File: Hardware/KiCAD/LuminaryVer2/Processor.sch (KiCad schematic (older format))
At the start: 18 parts, among them SW1 SW_Push, U2 STM32L432KBUx, U6 AT25SF081-SSHD-X

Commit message: Updated version 2 hardware schematics.
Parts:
- removed R_PWR_3: 0, Resistor_SMD:R_0402_1005Metric, symbol Device:R_US
- added C12, C14: 1uF, Capacitor_SMD:C_0805_2012Metric, symbol Device:C_Small
- added D3, D4: BLED, Diode_SMD:D_0603_1608Metric, symbol Device:LED
- added R16, R17, R18: 1k, Resistor_SMD:R_0402_1005Metric, symbol Device:R_US
- added U10: CP2104, Package_DFN_QFN:QFN-24-1EP_4x4mm_P0.5mm_EP2.6x2.6mm, symbol Interface_USB:CP2104
- D10: LCSC C205443 -> C72043; PartNumber ORH-G36G -> 19-217/GHC-YR1S2/3T
- R11, R3, R32: LCSC C102759 -> C25744
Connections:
- net GND: now also C12.1, C14.2, U10.2 (GND), U10.25 (PAD)
- net RS232_1_RX: now also U10.21 (TXD)
- net RS232_1_TX: now also U10.20 (RXD)
- net VCC: now also C2.2, U6.3 (~WP~/IO2), U6.7 (~HOLD~/IO3), U6.8 (VCC)
- new net: C14.1, R18.2, U10.10 (VIO/NC), U10.5 (VIO), U10.6 (VDD)
- new net: R16.1, U10.13 (GPIO.1)
- new net: R17.1, U10.14 (GPIO.0)
- new net: R18.1, U10.9 (~RST)
- new net: D4.1 (K), R17.2
- new net: D3.1 (K), R16.2
- new net D+: U10.3 (D+)
- new net D-: U10.4 (D-)
- new net USB+5v: C12.2, D3.2 (A), D4.2 (A), U10.7 (REGIN), U10.8 (VBUS)
- no-connect marks 0 -> 11
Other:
- note added: "Processor"
- note added: "System Flash Memory"
- note added: "USB to Serial Converter"
- moved on the sheet: C1, C2, C3, C4, D10, R1, R11, R2, R3, R32, R4, R5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

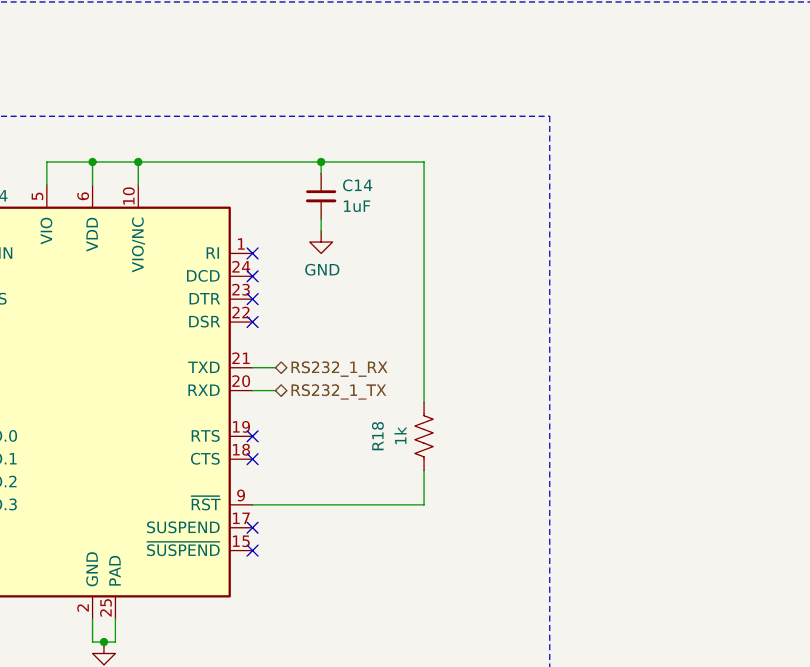
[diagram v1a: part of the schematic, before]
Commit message: Version two nets fully routed.
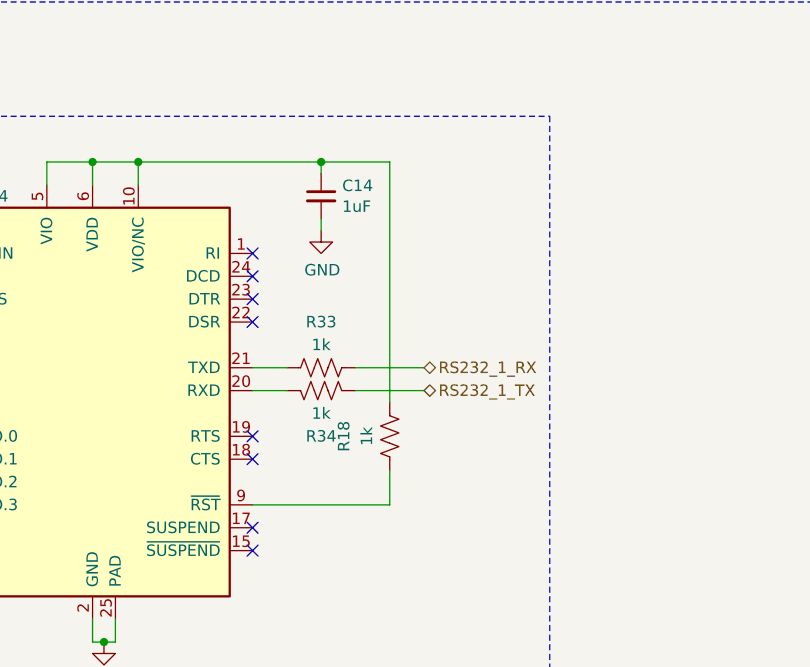
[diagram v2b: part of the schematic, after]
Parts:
- added R33, R34: 1k, Resistor_SMD:R_0402_1005Metric, symbol Device:R_US
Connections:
- net RS232_1_RX: now also R33.2; no longer U10.21 (TXD)
- net RS232_1_TX: now also R34.2; no longer U10.20 (RXD)
- new net: R33.1, U10.21 (TXD)
- new net: R34.1, U10.20 (RXD)
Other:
- moved on the sheet: R18
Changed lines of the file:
@@
 	-1   0    0    1
 $EndComp
-Text HLabel 4300 5700 2    50   BiDi ~ 0
+Text HLabel 4950 5700 2    50   BiDi ~ 0
 RS232_1_TX
-Text HLabel 4300 5600 2    50   BiDi ~ 0
+Text HLabel 4950 5600 2    50   BiDi ~ 0
 RS232_1_RX
 Text HLabel 2700 5700 0    50   BiDi ~ 0
@@
 L Device:R_US R?
 U 1 1 5EF75F53
-P 4950 5900
+P 4800 5900
 AR Path="/5E5FC17D/5EF75F53" Ref="R?"  Part="1"
 AR Path="/5E5FC13E/5EF75F53" Ref="R?"  Part="1"
 AR Path="/5E5FC1C1/5EF75F53" Ref="R18"  Part="1"
-F 0 "R18" V 5150 5900 50  0000 C CNN
-F 1 "1k" V 5050 5900 50  0000 C CNN
-F 2 "Resistor_SMD:R_0402_1005Metric" V 4990 5890 50  0001 C CNN
-F 3 "~" H 4950 5900 50  0001 C CNN
-F 4 "C11702" H 4950 5900 50  0001 C CNN "LCSC"
-F 5 "0402WGF4702TCE" H 4950 5900 50  0001 C CNN "PartNumber"
-	1    4950 5900
-	-1   0    0    1
-$EndComp
-Wire Wire Line
-	4950 6050 4950 6200
-Wire Wire Line
-	4950 6200 4200 6200
-Wire Wire Line
-	4950 5750 4950 4700
-Wire Wire Line
-	4950 4700 4500 4700
+F 0 "R18" V 5000 5900 50  0000 C CNN
+F 1 "1k" V 4900 5900 50  0000 C CNN
+F 2 "Resistor_SMD:R_0402_1005Metric" V 4840 5890 50  0001 C CNN
+F 3 "~" H 4800 5900 50  0001 C CNN
+F 4 "C11702" H 4800 5900 50  0001 C CNN "LCSC"
+F 5 "0402WGF4702TCE" H 4800 5900 50  0001 C CNN "PartNumber"
+	1    4800 5900
+	-1   0    0    1
+$EndComp
 Connection ~ 3700 4700
 Text HLabel 1600 4700 0    50   BiDi ~ 0
@@
 Wire Wire Line
 	2700 5700 2800 5700
-Wire Wire Line
-	4300 5600 4200 5600
-Wire Wire Line
-	4200 5700 4300 5700
 $Comp
 L Device:C_Small C?
@@
 Wire Wire Line
 	4500 4750 4500 4700
-Connection ~ 4500 4700
 Wire Wire Line
 	4500 4700 3700 4700
@@
 Text Notes 1000 1000 0    50   ~ 0
 Processor
+$Comp
+L Device:R_US R?
+U 1 1 5EE1B61C
+P 4500 5600
+AR Path="/5E5FC17D/5EE1B61C" Ref="R?"  Part="1"
+AR Path="/5E5FC13E/5EE1B61C" Ref="R?"  Part="1"
+AR Path="/5E5FC1C1/5EE1B61C" Ref="R33"  Part="1"
+F 0 "R33" V 4700 5600 50  0000 C CNN
+F 1 "1k" V 4600 5600 50  0000 C CNN
+F 2 "Resistor_SMD:R_0402_1005Metric" V 4540 5590 50  0001 C CNN
+F 3 "~" H 4500 5600 50  0001 C CNN
+F 4 "C11702" H 4500 5600 50  0001 C CNN "LCSC"
+F 5 "0402WGF4702TCE" H 4500 5600 50  0001 C CNN "PartNumber"
+	1    4500 5600
+	0    -1   -1   0
+$EndComp
+$Comp
+L Device:R_US R?
+U 1 1 5EE1BAE7
+P 4500 5700
+AR Path="/5E5FC17D/5EE1BAE7" Ref="R?"  Part="1"
+AR Path="/5E5FC13E/5EE1BAE7" Ref="R?"  Part="1"
+AR Path="/5E5FC1C1/5EE1BAE7" Ref="R34"  Part="1"
+F 0 "R34" V 4700 5700 50  0000 C CNN
+F 1 "1k" V 4600 5700 50  0000 C CNN
+F 2 "Resistor_SMD:R_0402_1005Metric" V 4540 5690 50  0001 C CNN
+F 3 "~" H 4500 5700 50  0001 C CNN
+F 4 "C11702" H 4500 5700 50  0001 C CNN "LCSC"
+F 5 "0402WGF4702TCE" H 4500 5700 50  0001 C CNN "PartNumber"
+	1    4500 5700
+	0    -1   1    0
+$EndComp
+Wire Wire Line
+	4200 5700 4350 5700
+Wire Wire Line
+	4200 5600 4350 5600
+Wire Wire Line
+	4800 5750 4800 4700
+Wire Wire Line
+	4800 4700 4500 4700
+Connection ~ 4500 4700
+Wire Wire Line
+	4800 6050 4800 6200
+Wire Wire Line
+	4800 6200 4200 6200
+Wire Wire Line
+	4950 5700 4650 5700
+Wire Wire Line
+	4950 5600 4650 5600
 $EndSCHEMATC
